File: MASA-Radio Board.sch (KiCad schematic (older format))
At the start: 58 parts, among them IC1 FAN4010IL6X_F113, IC2 FAN4010IL6X_F113, J1 Conn_01x02, J2 Conn_01x02_Male, J3 Conn_01x02_Male, J4 Conn_01x03_Male, J5 Conn_01x06, J6 SC_19-20, J7 Conn_01x06, J8 Conn_01x02, J9 UJ2-MBH-1-SMT-TR, U1 MP5077GG-Z, U2 BL654PA, U3 MIC5504-3.3YM5, U4 MP5077GG-Z

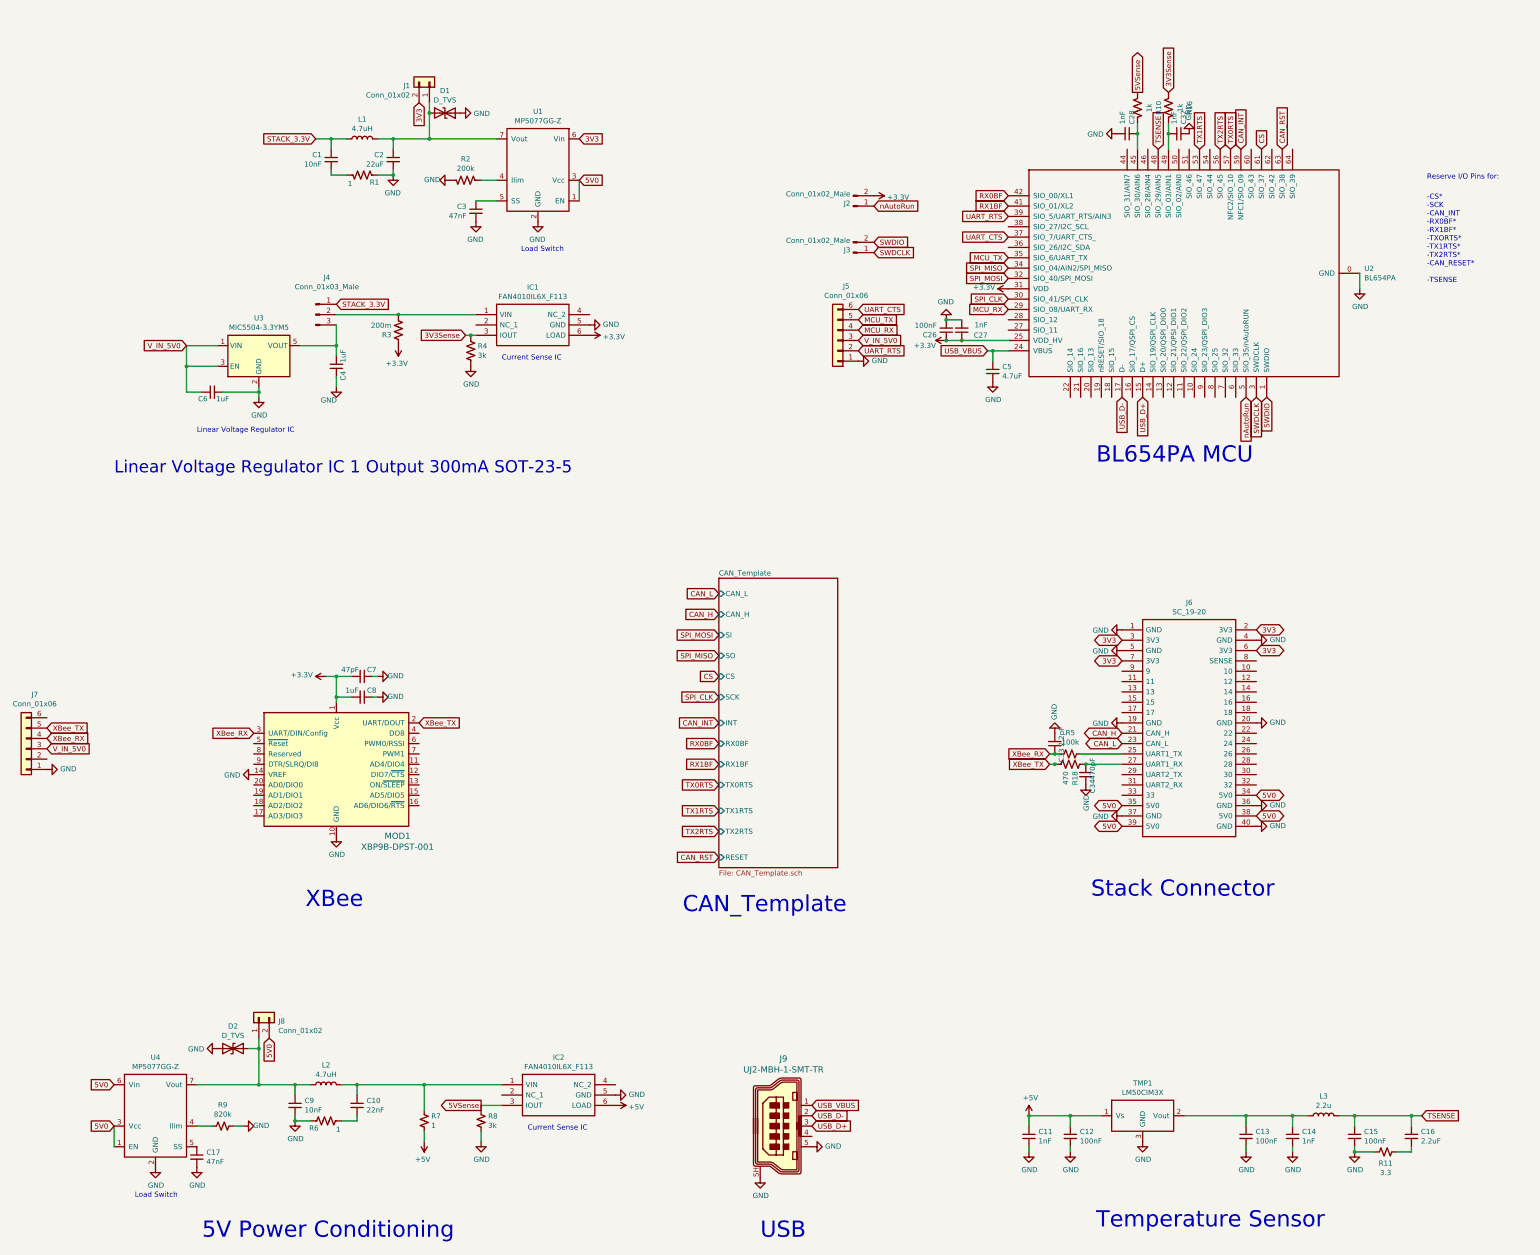
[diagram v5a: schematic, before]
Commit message: Added test points
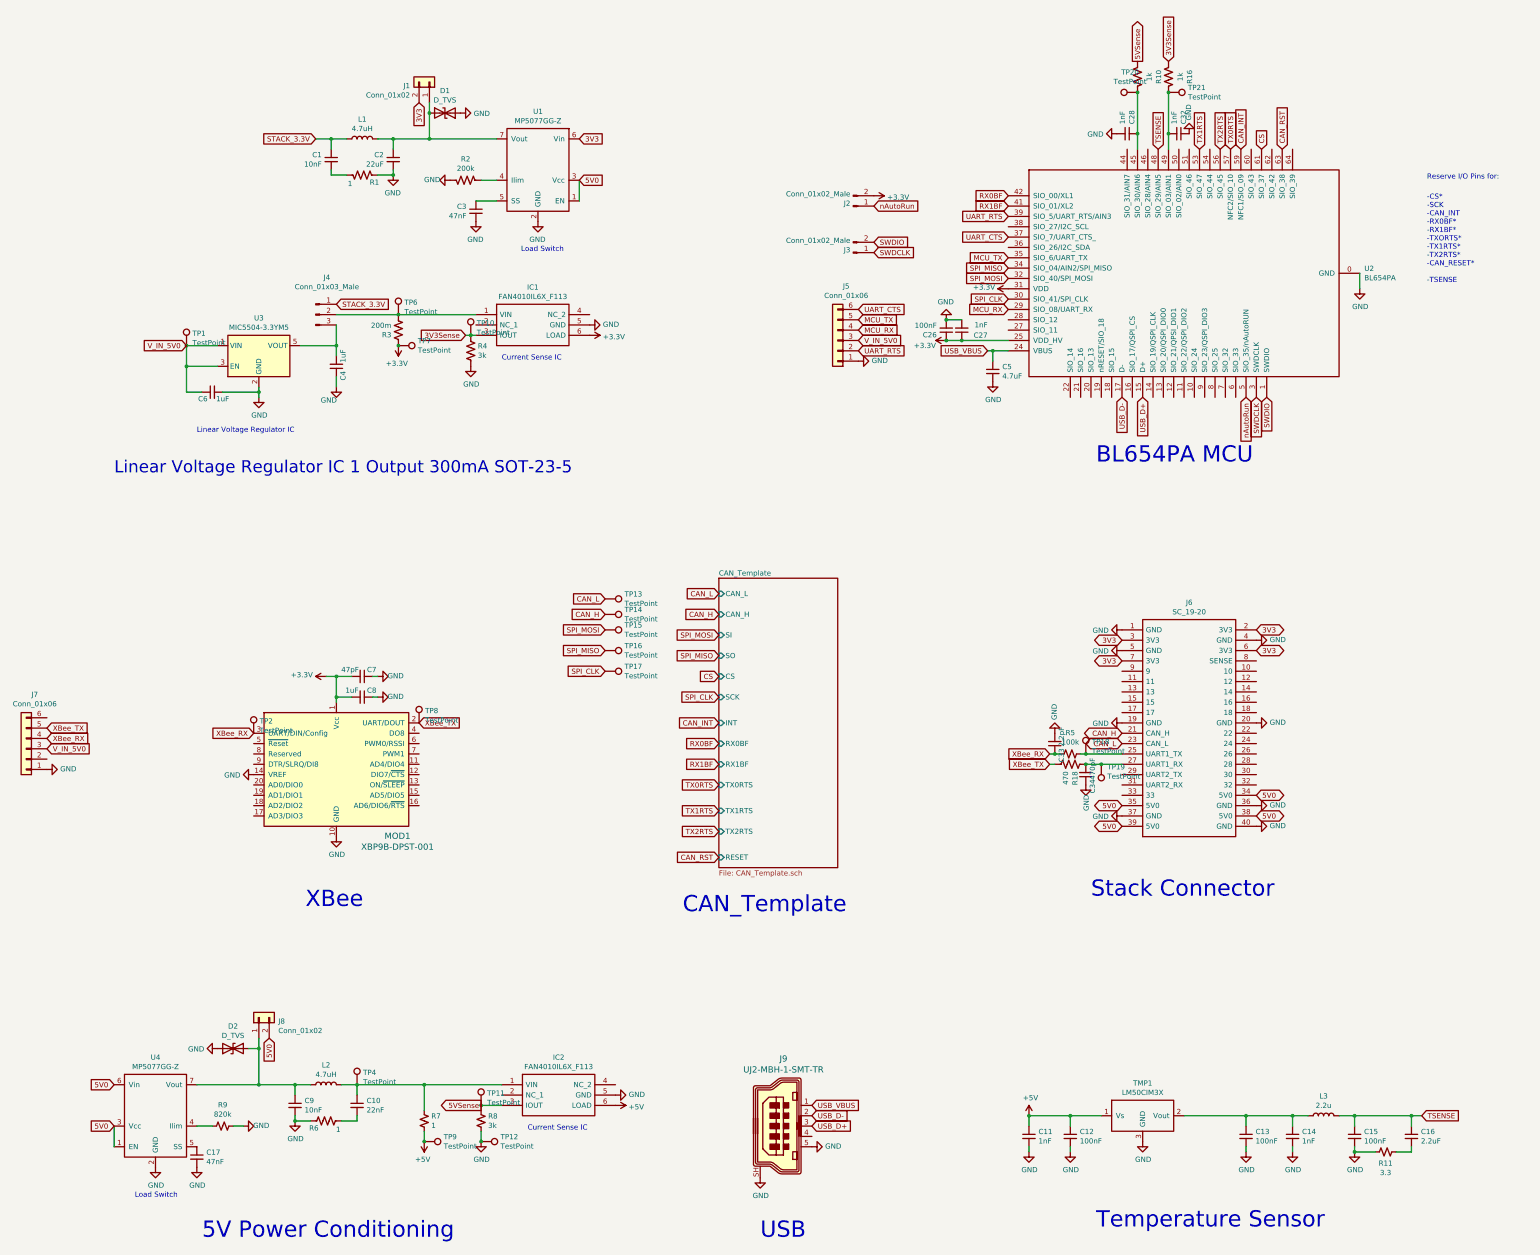
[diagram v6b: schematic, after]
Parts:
- added TP1, TP10, TP11, TP12, TP13, TP14, TP15, TP16, TP17, TP18, TP19, TP2, TP20, TP21, TP4, TP6, TP7, TP8, TP9: TestPoint, TestPoint:TestPoint_Pad_1.0x1.0mm, symbol Connector:TestPoint
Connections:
- net +3V3: now also TP7.1
- net +5V: now also TP9.1
- net 3V3Sense: now also TP10.1
- net 5VSense: now also TP11.1
- net CAN_H: now also TP14.1
- net CAN_L: now also TP13.1
- net GND: now also TP12.1
- net SPI_CLK: now also TP17.1
- net SPI_MISO: now also TP16.1
- net SPI_MOSI: now also TP15.1
- net V_IN_5V0: now also TP1.1
- net XBee_RX: now also TP2.1
- net XBee_TX: now also TP8.1
- net at J6.25 (UART1_TX), R5.1: now also TP18.1
- net at C34.2, J6.27 (UART1_RX), R18.1: now also TP19.1
- net at IC1.1 (VIN), J4.2 (Pin_2), R3.2: now also TP6.1
- net at C28.1, R10.2, U2.45 (SIO_30/AIN6): now also TP20.1
- net at C32.2, R16.2, U2.49 (SIO_03/AIN1): now also TP21.1
- net at C10.1, IC2.1 (VIN), L2.2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: now also TP4.1
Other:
- moved on the sheet: R10, R16

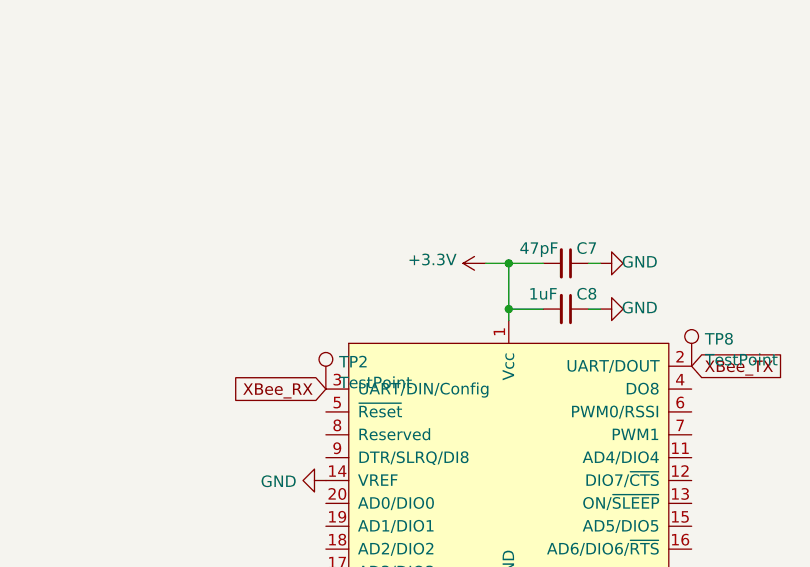
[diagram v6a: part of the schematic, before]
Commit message: Added 0 Ohm resistors
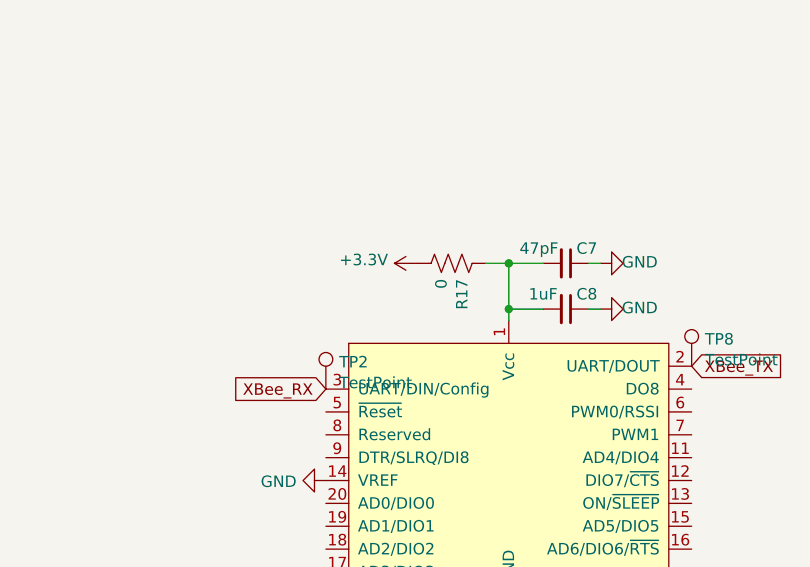
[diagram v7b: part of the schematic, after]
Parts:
- added R17: 0, Resistor_SMD:R_0603_1608Metric, symbol Device:R_US
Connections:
- net +3V3: now also R17.2; no longer C7.2, C8.2, MOD1.1 (Vcc)
- new net: C7.2, C8.2, MOD1.1 (Vcc), R17.1
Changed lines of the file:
@@
 L power:+3.3V #PWR020
 U 1 1 5E2C3468
-P 4850 7650
-F 0 "#PWR020" H 4850 7500 50  0001 C CNN
-F 1 "+3.3V" V 4865 7778 50  0000 L CNN
-F 2 "" H 4850 7650 50  0001 C CNN
-F 3 "" H 4850 7650 50  0001 C CNN
-	1    4850 7650
+P 4550 7650
+F 0 "#PWR020" H 4550 7500 50  0001 C CNN
+F 1 "+3.3V" V 4565 7778 50  0000 L CNN
+F 2 "" H 4550 7650 50  0001 C CNN
+F 3 "" H 4550 7650 50  0001 C CNN
+	1    4550 7650
 	0    -1   -1   0
 $EndComp
@@
 	0    1    1    0
 $EndComp
+$Comp
+L Device:R_US R17
+U 1 1 5E36278C
+P 4700 7650
+F 0 "R17" H 4768 7696 50  0000 L CNN
+F 1 "0" H 4768 7605 50  0000 L CNN
+F 2 "Resistor_SMD:R_0603_1608Metric" V 4740 7640 50  0001 C CNN
+F 3 "~" H 4700 7650 50  0001 C CNN
+	1    4700 7650
+	0    1    1    0
+$EndComp

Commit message: Updated silk screen
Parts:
- L1, L2: footprint Inductor_SMD:L_0603_1608Metric -> Inductor_SMD:L_0805_2012Metric
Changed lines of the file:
@@
 F 0 "L1" V 5390 2450 50  0000 C CNN
 F 1 "4.7uH" V 5299 2450 50  0000 C CNN
-F 2 "Inductor_SMD:L_0603_1608Metric" H 5200 2450 50  0001 C CNN
+F 2 "Inductor_SMD:L_0805_2012Metric" H 5200 2450 50  0001 C CNN
 F 3 "~" H 5200 2450 50  0001 C CNN
 	1    5200 2450
@@
 F 0 "L2" V 5040 11600 50  0000 C CNN
 F 1 "4.7uH" V 4949 11600 50  0000 C CNN
-F 2 "Inductor_SMD:L_0603_1608Metric" H 4850 11600 50  0001 C CNN
+F 2 "Inductor_SMD:L_0805_2012Metric" H 4850 11600 50  0001 C CNN
 F 3 "~" H 4850 11600 50  0001 C CNN
 	1    4850 11600
